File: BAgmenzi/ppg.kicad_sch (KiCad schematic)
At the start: 10 parts, among them U9 MAXM86161EFD_T

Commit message: added libraries, other changes in sch, started pcb
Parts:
- renumbered C43 to C44, C44 to C45, C45 to C46
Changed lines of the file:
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@@
-		)
-	)
-	(global_label "PPG_I2C{SCL, SDA}"
-		(shape bidirectional)
-		(at 213.36 83.82 0)
-		(fields_autoplaced yes)
-		(effects
-			(font
-				(size 1.27 1.27)
-			)
-			(justify left)
-		)
-		(property "Intersheetrefs" "${INTERSHEET_REFS}"
-			(at 235.6599 83.82 0)
-			(effects
-				(font
-					(size 1.27 1.27)
-				)
-				(justify left)
-			)
 		)
 	)
@@
 		)
 	)
+	(hierarchical_label "PPG_I2C{SCL, SDA}"
+		(shape bidirectional)
+		(at 213.36 83.82 0)
+		(effects
+			(font
+				(size 1.27 1.27)
+			)
+			(justify left)
+		)
+	)
 	(symbol
 		(lib_id "power:GND")
@@
 		(on_board yes)
 		(dnp no)
-		(property "Reference" "C44"
+		(property "Reference" "C45"
 			(at 82.55 90.932 90)
 			(effects
@@
 			(project ""
 				(path "/8cc4acae-3f14-463c-b0a0-3bc1c8d05954/af15e2f0-2c1b-4135-9358-6031ad08c9a3"
-					(reference "C44")
+					(reference "C45")
 					(unit 1)
 				)
@@
 		(on_board yes)
 		(dnp no)
-		(property "Reference" "C45"
+		(property "Reference" "C46"
 			(at 82.042 103.378 90)
 			(effects
@@
 			(project "BAgmenzi"
 				(path "/8cc4acae-3f14-463c-b0a0-3bc1c8d05954/af15e2f0-2c1b-4135-9358-6031ad08c9a3"
-					(reference "C45")
+					(reference "C46")
 					(unit 1)
 				)
@@
 		(on_board yes)
 		(dnp no)
-		(property "Reference" "C43"
+		(property "Reference" "C44"
 			(at 50.038 98.298 90)
 			(effects
@@
 			(project "BAgmenzi"
 				(path "/8cc4acae-3f14-463c-b0a0-3bc1c8d05954/af15e2f0-2c1b-4135-9358-6031ad08c9a3"
-					(reference "C43")
-					(unit 1)
-				)
+					(reference "C44")
+					(unit 1)
+				)

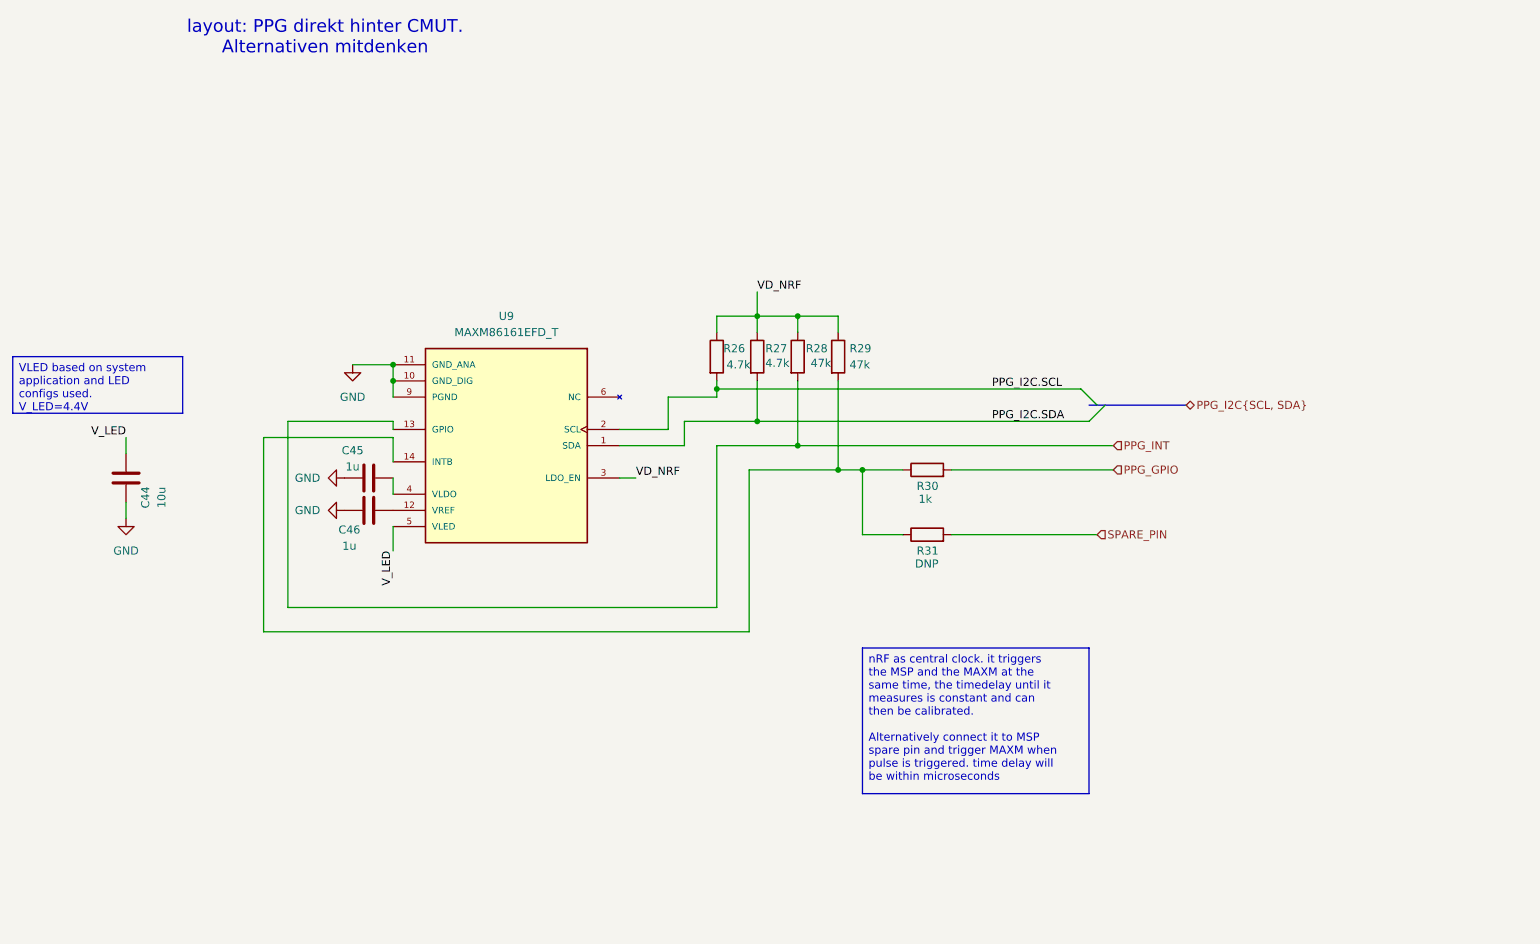
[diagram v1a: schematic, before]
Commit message: changed VRX rail and deleted U12
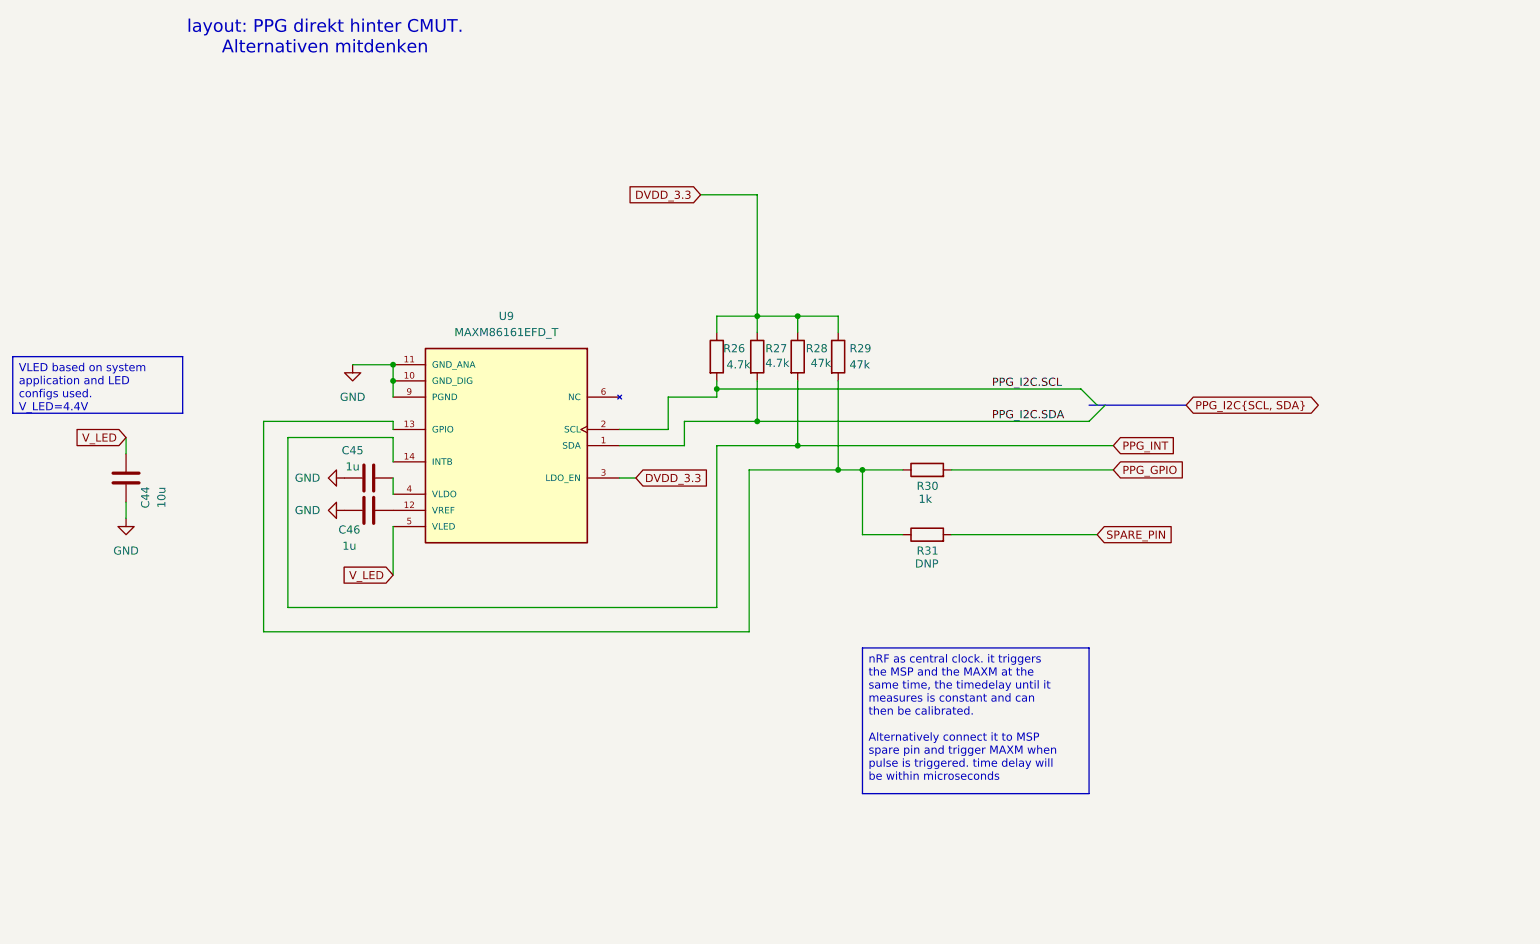
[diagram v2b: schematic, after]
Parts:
- C44, C45, C46: footprint (none) -> Capacitor_SMD:C_0402_1005Metric
- R26, R27, R28, R29, R30, R31: footprint (none) -> Resistor_SMD:R_0402_1005Metric
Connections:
- net PPG_INT: now also U9.14 (INTB); no longer U9.13 (GPIO)
- net at R29.2, R30.1, R31.1: now also U9.13 (GPIO); no longer U9.14 (INTB)
- net VD_NRF renamed DVDD_3.3
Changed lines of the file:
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@@
+	(wire
+		(pts
+			(xy 72.39 115.57) (xy 72.39 88.9)
+		)
+		(stroke
+			(width 0)
+			(type default)
+		)
+	)
 	(wire
 		(pts
@@
 	(wire
 		(pts
-			(xy 88.9 86.36) (xy 72.39 86.36)
-		)
-		(stroke
-			(width 0)
-			(type default)
-		)
-	)
-	(wire
-		(pts
-			(xy 72.39 86.36) (xy 72.39 115.57)
+			(xy 137.16 50.8) (xy 146.05 50.8)
 		)
 		(stroke
@@
 	(wire
 		(pts
+			(xy 72.39 88.9) (xy 88.9 88.9)
+		)
+		(stroke
+			(width 0)
+			(type default)
+		)
+	)
+	(wire
+		(pts
+			(xy 146.05 50.8) (xy 146.05 69.85)
+		)
+		(stroke
+			(width 0)
+			(type default)
+		)
+	)
+	(wire
+		(pts
 			(xy 162.56 104.14) (xy 162.56 93.98)
 		)
@@
 	(wire
 		(pts
-			(xy 68.58 88.9) (xy 68.58 119.38)
+			(xy 68.58 86.36) (xy 68.58 119.38)
 		)
 		(stroke
@@
 	(wire
 		(pts
+			(xy 68.58 86.36) (xy 88.9 86.36)
+		)
+		(stroke
+			(width 0)
+			(type default)
+		)
+	)
+	(wire
+		(pts
 			(xy 139.7 115.57) (xy 139.7 90.17)
 		)
@@
 	(wire
 		(pts
-			(xy 88.9 88.9) (xy 68.58 88.9)
-		)
-		(stroke
-			(width 0)
-			(type default)
-		)
-	)
-	(wire
-		(pts
 			(xy 46.99 91.44) (xy 46.99 88.9)
 		)
@@
 	(wire
 		(pts
-			(xy 88.9 106.68) (xy 88.9 102.87)
-		)
-		(stroke
-			(width 0)
-			(type default)
-		)
-	)
-	(wire
-		(pts
 			(xy 139.7 80.01) (xy 139.7 81.28)
 		)
@@
 	(wire
 		(pts
-			(xy 146.05 66.04) (xy 146.05 69.85)
-		)
-		(stroke
-			(width 0)
-			(type default)
-		)
-	)
-	(wire
-		(pts
 			(xy 152.4 69.85) (xy 152.4 72.39)
 		)
@@
 	(wire
 		(pts
+			(xy 88.9 102.87) (xy 88.9 110.49)
+		)
+		(stroke
+			(width 0)
+			(type default)
+		)
+	)
+	(wire
+		(pts
 			(xy 88.9 88.9) (xy 88.9 92.71)
 		)
@@
 			(width 0)
 			(type default)
-		)
-	)
-	(label "VD_NRF"
-		(at 127 95.25 0)
-		(effects
-			(font
-				(size 1.27 1.27)
-			)
-			(justify left bottom)
-		)
-	)
-	(label "V_LED"
-		(at 88.9 106.68 270)
-		(effects
-			(font
-				(size 1.27 1.27)
-			)
-			(justify right bottom)
-		)
-	)
-	(label "VD_NRF"
-		(at 146.05 66.04 0)
-		(effects
-			(font
-				(size 1.27 1.27)
-			)
-			(justify left bottom)
-		)
-	)
-	(label "V_LED"
-		(at 46.99 88.9 180)
-		(effects
-			(font
-				(size 1.27 1.27)
-			)
-			(justify right bottom)
 		)
 	)
@@
 		)
 	)
-	(hierarchical_label "PPG_INT"
+	(global_label "SPARE_PIN"
 		(shape input)
-		(at 201.93 90.17 0)
+		(at 199.39 104.14 0)
+		(fields_autoplaced yes)
 		(effects
 			(font
@@
 			(justify left)
 		)
-	)
-	(hierarchical_label "PPG_GPIO"
-		(shape input)
-		(at 201.93 93.98 0)
+		(property "Intersheetrefs" "${INTERSHEET_REFS}"
+			(at 212.5352 104.14 0)
+			(effects
+				(font
+					(size 1.27 1.27)
+				)
+				(justify left)
+			)
+		)
+	)
+	(global_label "PPG_I2C{SCL, SDA}"
+		(shape bidirectional)
+		(at 213.36 83.82 0)
+		(fields_autoplaced yes)
 		(effects
 			(font
@@
 			(justify left)
 		)
-	)
-	(hierarchical_label "SPARE_PIN"
+		(property "Intersheetrefs" "${INTERSHEET_REFS}"
+			(at 235.6599 83.82 0)
+			(effects
+				(font
+					(size 1.27 1.27)
+				)
+				(justify left)
+			)
+		)
+	)
+	(global_label "V_LED"
 		(shape input)
-		(at 199.39 104.14 0)
+		(at 46.99 88.9 180)
+		(fields_autoplaced yes)
 		(effects
 			(font
 				(size 1.27 1.27)
 			)
-			(justify left)
-		)
-	)
-	(hierarchical_label "PPG_I2C{SCL, SDA}"
-		(shape bidirectional)
-		(at 213.36 83.82 0)
+			(justify right)
+		)
+		(property "Intersheetrefs" "${INTERSHEET_REFS}"
+			(at 38.5015 88.9 0)
+			(effects
+				(font
+					(size 1.27 1.27)
+				)
+				(justify right)
+			)
+		)
+	)
+	(global_label "PPG_GPIO"
+		(shape input)
+		(at 201.93 93.98 0)
+		(fields_autoplaced yes)
 		(effects
 			(font
@@
 			)
 			(justify left)
+		)
+		(property "Intersheetrefs" "${INTERSHEET_REFS}"
+			(at 214.1681 93.98 0)
+			(effects
+				(font
+					(size 1.27 1.27)
+				)
+				(justify left)
+			)
+		)
+	)
+	(global_label "DVDD_3.3"
+		(shape input)
+		(at 127 95.25 0)
+		(fields_autoplaced yes)
+		(effects
+			(font
+				(size 1.27 1.27)
+			)
+			(justify left)
+		)
+		(property "Intersheetrefs" "${INTERSHEET_REFS}"
+			(at 138.8752 95.25 0)
+			(effects
+				(font
+					(size 1.27 1.27)
+				)
+				(justify left)
+			)
+		)
+	)
+	(global_label "PPG_INT"
+		(shape input)
+		(at 201.93 90.17 0)
+		(fields_autoplaced yes)
+		(effects
+			(font
+				(size 1.27 1.27)
+			)
+			(justify left)
+		)
+		(property "Intersheetrefs" "${INTERSHEET_REFS}"
+			(at 212.5957 90.17 0)
+			(effects
+				(font
+					(size 1.27 1.27)
+				)
+				(justify left)
+			)
+		)
+	)
+	(global_label "DVDD_3.3"
+		(shape input)
+		(at 137.16 50.8 180)
+		(fields_autoplaced yes)
+		(effects
+			(font
+				(size 1.27 1.27)
+			)
+			(justify right)
+		)
+		(property "Intersheetrefs" "${INTERSHEET_REFS}"
+			(at 125.2848 50.8 0)
+			(effects
+				(font
+					(size 1.27 1.27)
+				)
+				(justify right)
+			)
+		)
+	)
+	(global_label "V_LED"
+		(shape input)
+		(at 88.9 110.49 180)
+		(fields_autoplaced yes)
+		(effects
+			(font
+				(size 1.27 1.27)
+			)
+			(justify right)
+		)
+		(property "Intersheetrefs" "${INTERSHEET_REFS}"
+			(at 80.4115 110.49 0)
+			(effects
+				(font
+					(size 1.27 1.27)
+				)
+				(justify right)
+			)
 		)
 	)
@@
 			)
 		)
-		(property "Footprint" ""
+		(property "Footprint" "Capacitor_SMD:C_0402_1005Metric"
 			(at 88.9 94.2848 0)
 			(effects
@@
 			)
 		)
-		(property "Footprint" ""
+		(property "Footprint" "Capacitor_SMD:C_0402_1005Metric"
 			(at 88.9 99.3648 0)
 			(effects
@@
 			)
 		)
-		(property "Footprint" ""
+		(property "Footprint" "Resistor_SMD:R_0402_1005Metric"
 			(at 137.922 76.2 90)
 			(effects
@@
 			)
 		)
-		(property "Footprint" ""
+		(property "Footprint" "Resistor_SMD:R_0402_1005Metric"
 			(at 156.972 76.2 90)
 			(effects
@@
 			)
 		)
-		(property "Footprint" ""
+		(property "Footprint" "Resistor_SMD:R_0402_1005Metric"
 			(at 150.622 76.2 90)
 			(effects
@@
 			)
 		)
-		(property "Footprint" ""
+		(property "Footprint" "Resistor_SMD:R_0402_1005Metric"
 			(at 172.72 105.918 90)
 			(effects
@@
 			)
 		)
-		(property "Footprint" ""
+		(property "Footprint" "Resistor_SMD:R_0402_1005Metric"
 			(at 144.272 76.2 90)
 			(effects
@@
 			)
 		)
-		(property "Footprint" ""
+		(property "Footprint" "Resistor_SMD:R_0402_1005Metric"
 			(at 172.72 95.758 90)
 			(effects
@@
 			)
 		)
-		(property "Footprint" ""
+		(property "Footprint" "Capacitor_SMD:C_0402_1005Metric"
 			(at 46.0248 91.44 0)
 			(effects

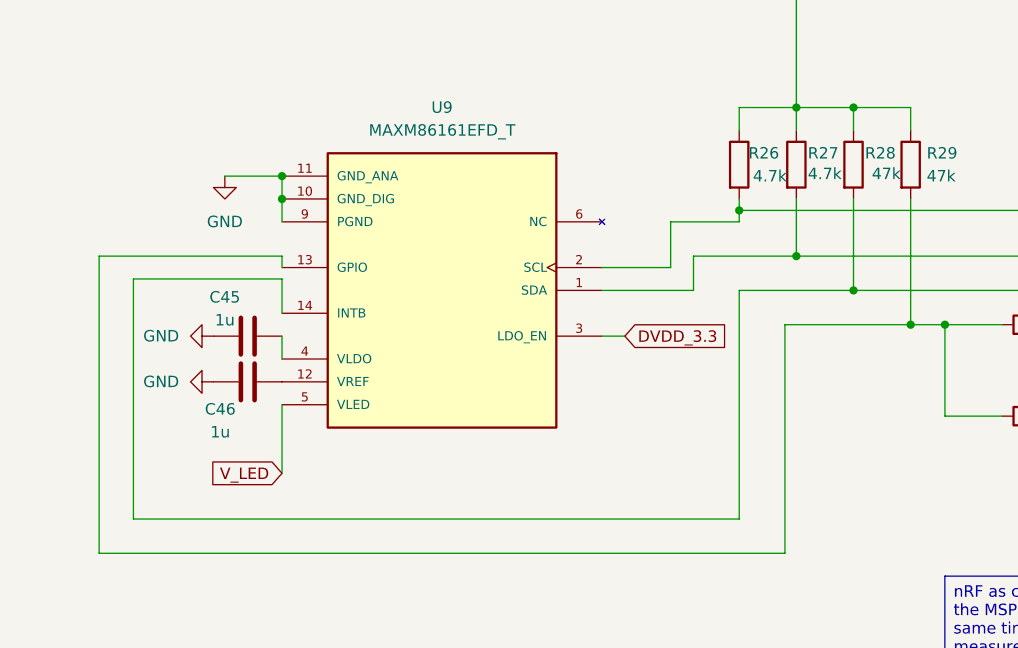
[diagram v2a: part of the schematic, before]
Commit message: added polyCMUT footprint, changed enables, more compact
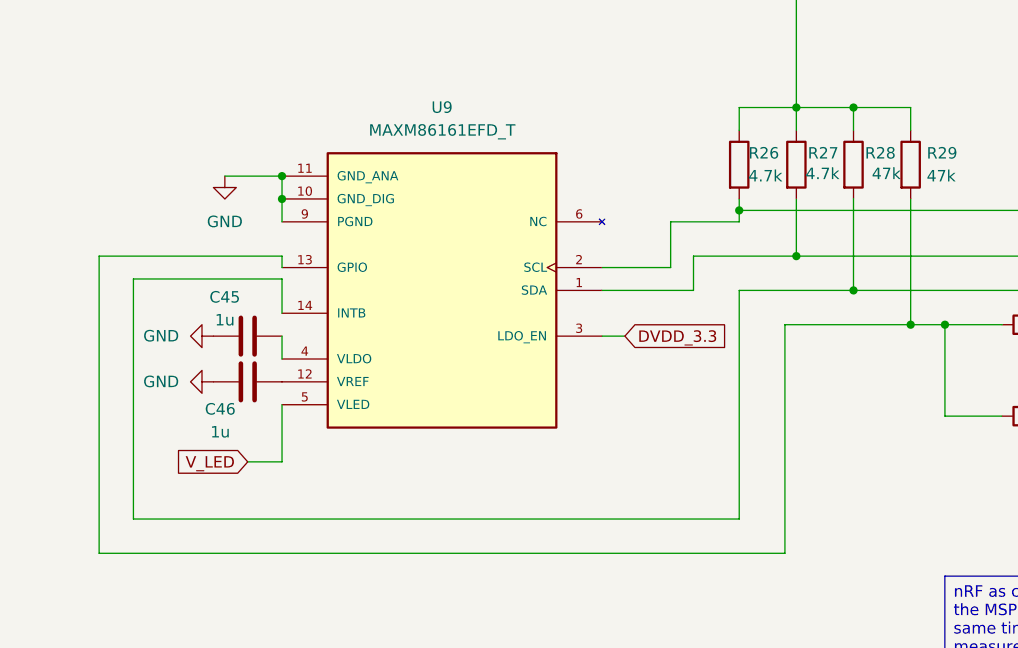
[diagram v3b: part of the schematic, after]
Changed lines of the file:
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@@
+	(wire
+		(pts
+			(xy 85.09 109.22) (xy 88.9 109.22)
+		)
+		(stroke
+			(width 0)
+			(type default)
+		)
+	)
 	(wire
 		(pts
@@
 		)
 	)
+	(wire
+		(pts
+			(xy 88.9 109.22) (xy 88.9 102.87)
+		)
+		(stroke
+			(width 0)
+			(type default)
+		)
+	)
 	(bus
 		(pts
@@
 		(pts
 			(xy 152.4 69.85) (xy 152.4 72.39)
-		)
-		(stroke
-			(width 0)
-			(type default)
-		)
-	)
-	(wire
-		(pts
-			(xy 88.9 102.87) (xy 88.9 110.49)
 		)
 		(stroke
@@
 	(global_label "V_LED"
 		(shape input)
-		(at 88.9 110.49 180)
+		(at 85.09 109.22 180)
 		(fields_autoplaced yes)
 		(effects
@@
 		)
 		(property "Intersheetrefs" "${INTERSHEET_REFS}"
-			(at 80.4115 110.49 0)
+			(at 76.6015 109.22 0)
 			(effects
 				(font
@@
 		)
 		(property "Value" "4.7k"
-			(at 141.224 77.47 0)
+			(at 140.716 77.47 0)
 			(effects
 				(font
@@
 		)
 		(property "Value" "4.7k"
-			(at 147.32 77.216 0)
-			(effects
-				(font
+			(at 147.066 77.216 0)
+			(effects
+				(font
